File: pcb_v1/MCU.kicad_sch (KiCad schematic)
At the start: 12 parts, among them U4 ESP32-S3-MINI-1, U6 STM32F103RETx

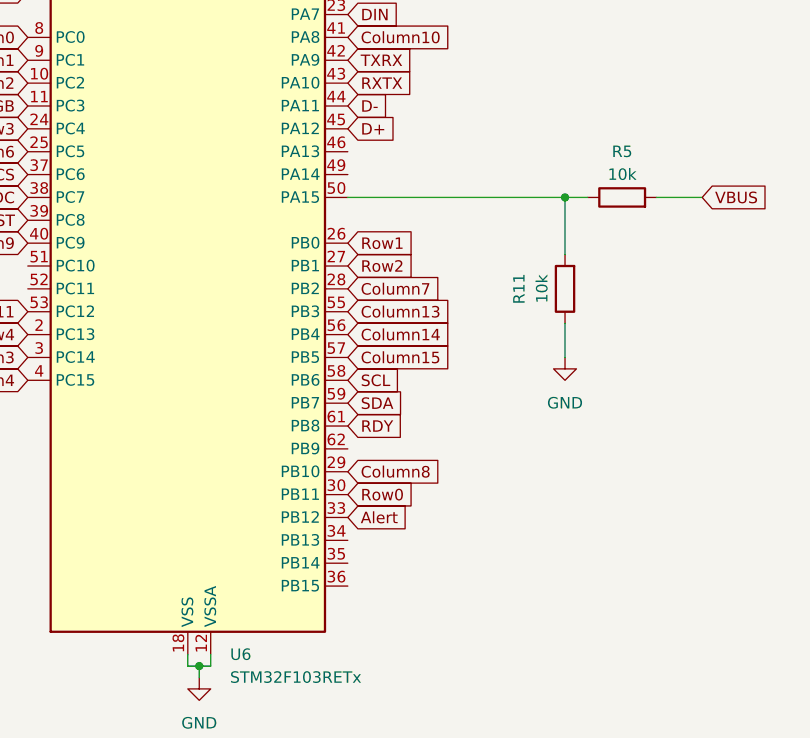
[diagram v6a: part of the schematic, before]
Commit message: New Charger IC, Added Ground Plane
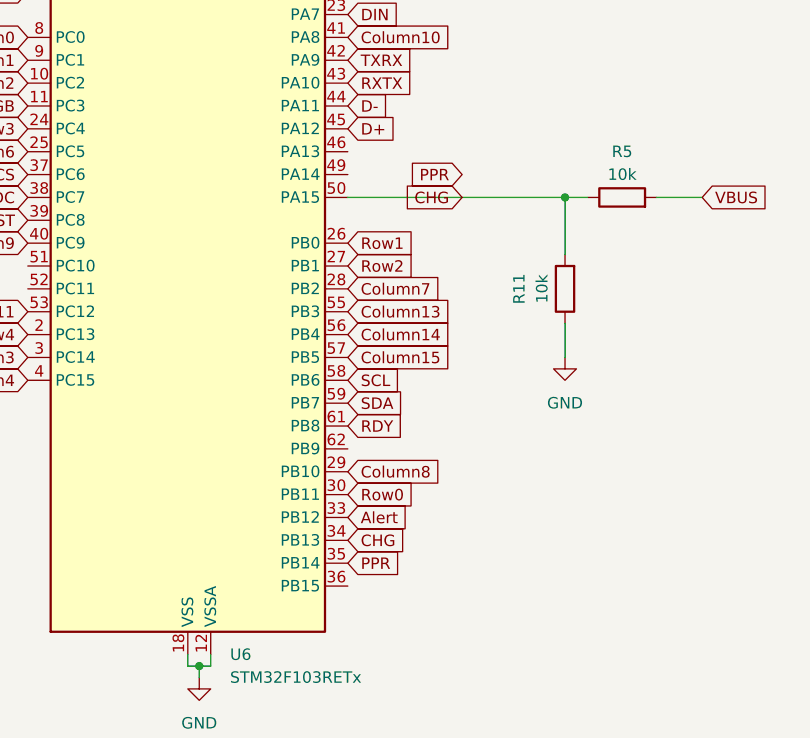
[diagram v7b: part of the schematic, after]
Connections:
- net CHG: now reaches U6.34 (PB13)
- net CHG: now also R11.2, R5.1, U6.50 (PA15)
- net PPR: now reaches U6.35 (PB14)
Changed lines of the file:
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@@
+		)
+	)
+	(global_label "PPR"
+		(shape input)
+		(at 162.56 156.21 0)
+		(fields_autoplaced yes)
+		(effects
+			(font
+				(size 1.27 1.27)
+			)
+			(justify left)
+		)
+		(property "Intersheetrefs" "${INTERSHEET_REFS}"
+			(at 169.3552 156.21 0)
+			(effects
+				(font
+					(size 1.27 1.27)
+				)
+				(justify left)
+				(hide yes)
+			)
 		)
 	)
@@
 		)
 	)
+	(global_label "CHG"
+		(shape input)
+		(at 162.56 153.67 0)
+		(fields_autoplaced yes)
+		(effects
+			(font
+				(size 1.27 1.27)
+			)
+			(justify left)
+		)
+		(property "Intersheetrefs" "${INTERSHEET_REFS}"
+			(at 169.4157 153.67 0)
+			(effects
+				(font
+					(size 1.27 1.27)
+				)
+				(justify left)
+				(hide yes)
+			)
+		)
+	)
 	(global_label "SCL"
 		(shape input)
@@
 		)
 	)
+	(global_label "CHG"
+		(shape input)
+		(at 175.26 115.57 180)
+		(fields_autoplaced yes)
+		(effects
+			(font
+				(size 1.27 1.27)
+			)
+			(justify right)
+		)
+		(property "Intersheetrefs" "${INTERSHEET_REFS}"
+			(at 168.4043 115.57 0)
+			(effects
+				(font
+					(size 1.27 1.27)
+				)
+				(justify right)
+				(hide yes)
+			)
+		)
+	)
 	(global_label "Column14"
 		(shape input)
@@
 			(effects
 				(font
+					(size 1.27 1.27)
+				)
+				(justify right)
+				(hide yes)
+			)
+		)
+	)
+	(global_label "PPR"
+		(shape input)
+		(at 175.26 113.03 180)
+		(fields_autoplaced yes)
+		(effects
+			(font
+				(size 1.27 1.27)
+			)
+			(justify right)
+		)
+		(property "Intersheetrefs" "${INTERSHEET_REFS}"
+			(at 168.4648 113.03 0)
+			(effects
+				(font

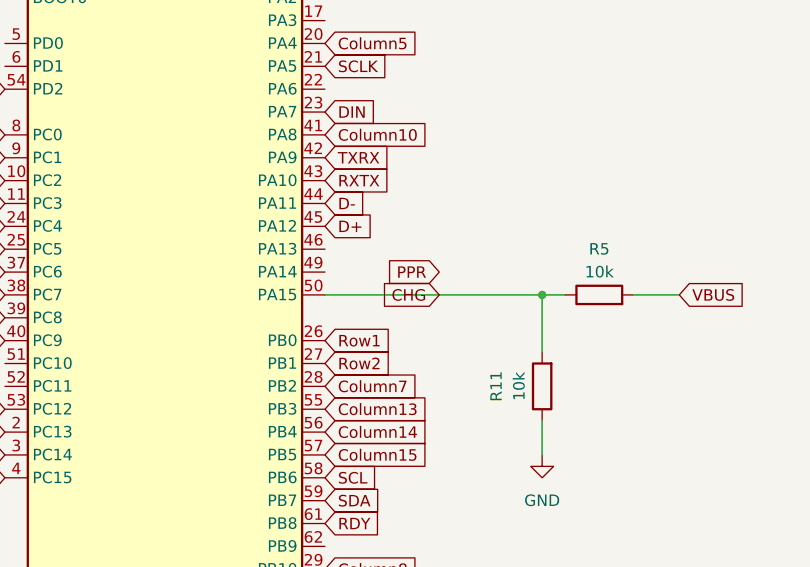
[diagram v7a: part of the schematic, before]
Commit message: Reposition IQS624
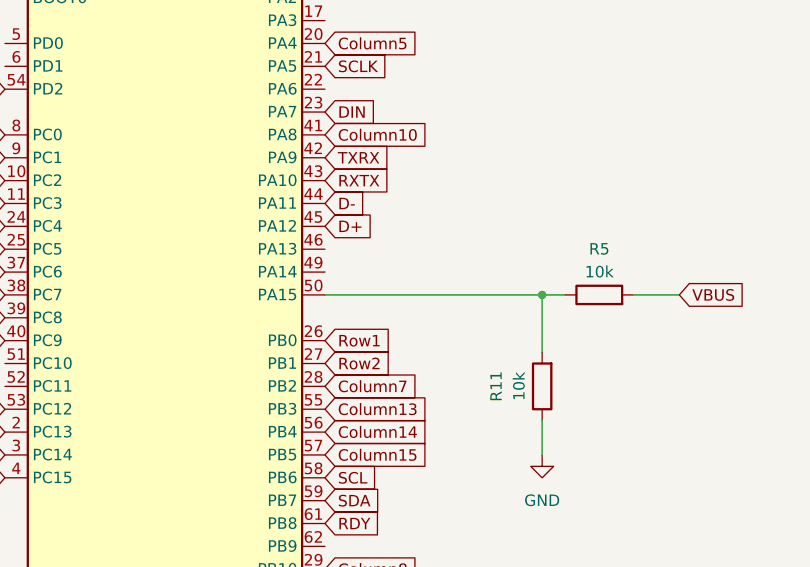
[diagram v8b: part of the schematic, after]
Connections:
- net CHG: no longer R11.2, R5.1, U6.50 (PA15)
- new net: R11.2, R5.1, U6.50 (PA15)
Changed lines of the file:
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@@
+	(wire
+		(pts
+			(xy 162.56 115.57) (xy 186.69 115.57)
+		)
+		(stroke
+			(width 0)
+			(type default)
+		)
+	)
 	(wire
 		(pts
@@
 	(wire
 		(pts
-			(xy 162.56 115.57) (xy 186.69 115.57)
-		)
-		(stroke
-			(width 0)
-			(type default)
-		)
-	)
-	(wire
-		(pts
 			(xy 142.24 68.58) (xy 142.24 69.85)
 		)
@@
 		)
 	)
-	(global_label "CHG"
-		(shape input)
-		(at 175.26 115.57 180)
-		(fields_autoplaced yes)
-		(effects
-			(font
-				(size 1.27 1.27)
-			)
-			(justify right)
-		)
-		(property "Intersheetrefs" "${INTERSHEET_REFS}"
-			(at 168.4043 115.57 0)
-			(effects
-				(font
-					(size 1.27 1.27)
-				)
-				(justify right)
-				(hide yes)
-			)
-		)
-	)
 	(global_label "Column14"
 		(shape input)
@@
 			(effects
 				(font
-					(size 1.27 1.27)
-				)
-				(justify right)
-				(hide yes)
-			)
-		)
-	)
-	(global_label "PPR"
-		(shape input)
-		(at 175.26 113.03 180)
-		(fields_autoplaced yes)
-		(effects
-			(font
-				(size 1.27 1.27)
-			)
-			(justify right)
-		)
-		(property "Intersheetrefs" "${INTERSHEET_REFS}"
-			(at 168.4648 113.03 0)
-			(effects
-				(font
